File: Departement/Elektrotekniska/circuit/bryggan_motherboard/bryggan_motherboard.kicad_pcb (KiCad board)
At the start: 2 copper layers, 68.6 x 74.9 mm, 8 parts, among them J1 Conn_01x02, J2 Conn_01x04, J3 RbPi connect, J4 Conn_01x04, J5 Conn_01x03, J6 Conn_01x03, U1 ULN2003

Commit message: KICAD clean
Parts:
- removed J6: Conn_01x03, Connectors_Terminal_Blocks:TerminalBlock_bornier-3_P5.08mm
- added REF**: 1pin, Connectors:1pin, F.Cu at (203.2, 74.9)
- added REF**: 1pin, Connectors:1pin, F.Cu at (142.2, 74.9)
- added REF**: 1pin, Connectors:1pin, F.Cu at (142.2, 142.2)
- added REF**: 1pin, Connectors:1pin, F.Cu at (203.2, 142.2)
- J1: footprint Connectors_Terminal_Blocks:TerminalBlock_bornier-2_P5.08mm -> TerminalBlocks_Phoenix:TerminalBlock_Phoenix_PT-3.5mm_2pol
- J2, J4: footprint Connectors_Terminal_Blocks:TerminalBlock_bornier-4_P5.08mm -> TerminalBlocks_Phoenix:TerminalBlock_Phoenix_PT-3.5mm_4pol
- J5: value Conn_01x03 -> RJ45; footprint Connectors_Terminal_Blocks:TerminalBlock_bornier-3_P5.08mm -> Connectors:RJ45_8
- moved J5 15.3 mm to (190.5, 94.0), turned to 90 degrees
- moved J4 10.2 mm to (184.2, 135.9), turned to 0 degrees
- moved J2 6.35 mm to (167.6, 135.9), turned to 0 degrees
- moved J1 3.81 mm to (148.6, 132.1), turned to 270 degrees
- moved R1 2.54 mm to (179.1, 85.1), turned to 270 degrees
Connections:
- J2 pad 1: Net-(J1-Pad1) -> Net-(J1-Pad2)
- J2 pad 2: Net-(J1-Pad1) -> Net-(J1-Pad2)
- J2 pad 3: Net-(J1-Pad1) -> Net-(J1-Pad2)
- J2 pad 4: Net-(J1-Pad1) -> Net-(J1-Pad2)
- J3 pad 10: Net-(J1-Pad2) -> Net-(J1-Pad1)
- J5 pad 1: Net-(J3-Pad5) -> Net-(J3-Pad1)
- J5 pad 2: Net-(J3-Pad3) -> Net-(J3-Pad1)
- J5 pad 3: Net-(J3-Pad1) -> Net-(J5-Pad3)
- R1 pad 1: Net-(J3-Pad3) -> Net-(J3-Pad5)
- R1 pad 2: Net-(J3-Pad5) -> Net-(J3-Pad3)
- U1 pad 10: Net-(J4-Pad4) -> Net-(J4-Pad1)
- U1 pad 11: Net-(J4-Pad3) -> Net-(J4-Pad2)
- U1 pad 12: Net-(J4-Pad2) -> Net-(J4-Pad3)
- U1 pad 13: Net-(J4-Pad1) -> Net-(J4-Pad4)
- U1 pad 8: Net-(J1-Pad2) -> Net-(J1-Pad1)
- U1 pad 9: Net-(J1-Pad1) -> Net-(J1-Pad2)
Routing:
- net Net-(J4-Pad1): track 33.0 -> 1.27 mm
- net Net-(J4-Pad2): track 30.5 -> 1.27 mm
- net Net-(J4-Pad3): track 27.9 -> 1.27 mm
- net Net-(J4-Pad4): track 25.4 -> 1.27 mm
- net Net-(J1-Pad2): track 47.1 -> 23.7 mm
- net Net-(J3-Pad5): track 42.4 -> 30.8 mm
- net Net-(J3-Pad3): track 34.1 -> 24.2 mm
- net Net-(J3-Pad1): track 26.5 -> 18.1 mm
- net (no net): track 2.54 -> 0.00 mm
- net Net-(J1-Pad1): track 49.1 -> 47.1 mm

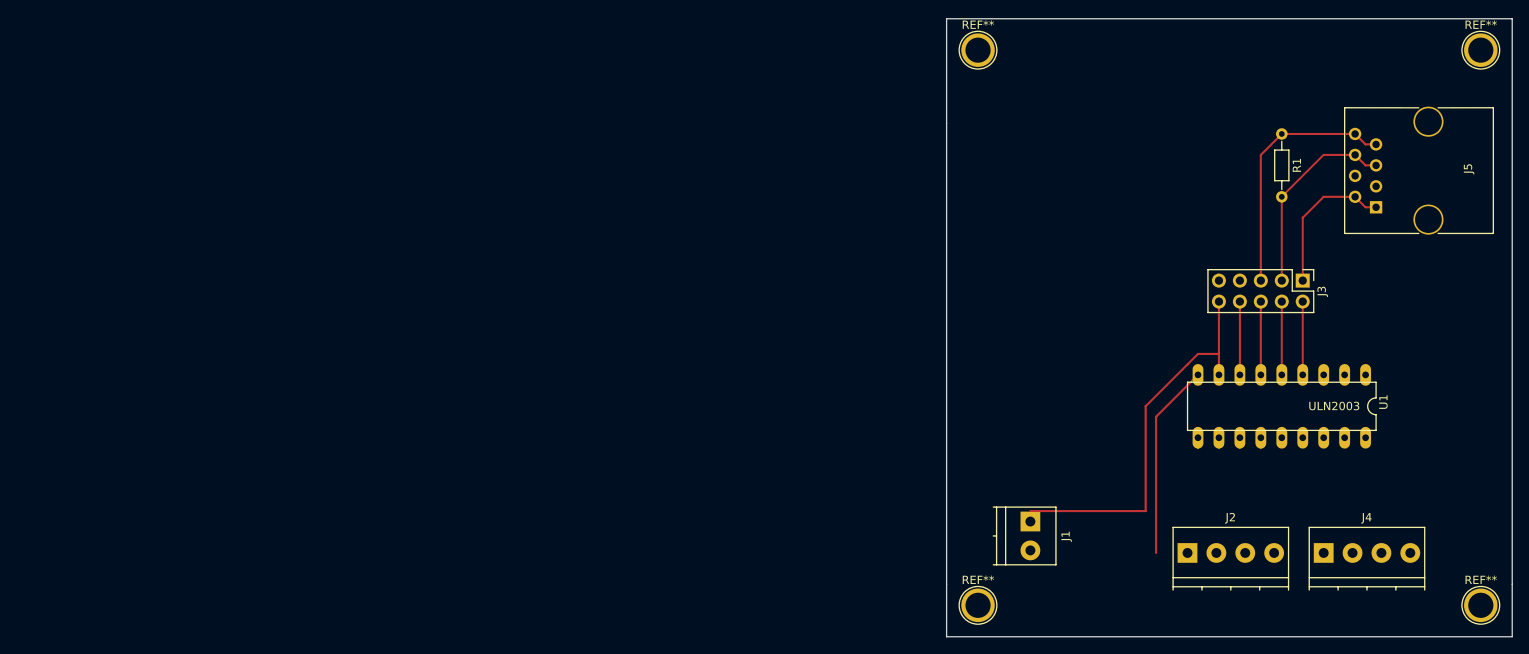
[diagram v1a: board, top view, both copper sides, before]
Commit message: RAW PIHAT TEMPLATE REMAKE
Template taken from: https://www.instructables.com/id/Design-a-Raspberry-Pi-Hat-KiCad/
No changes made, except replacing outdated components
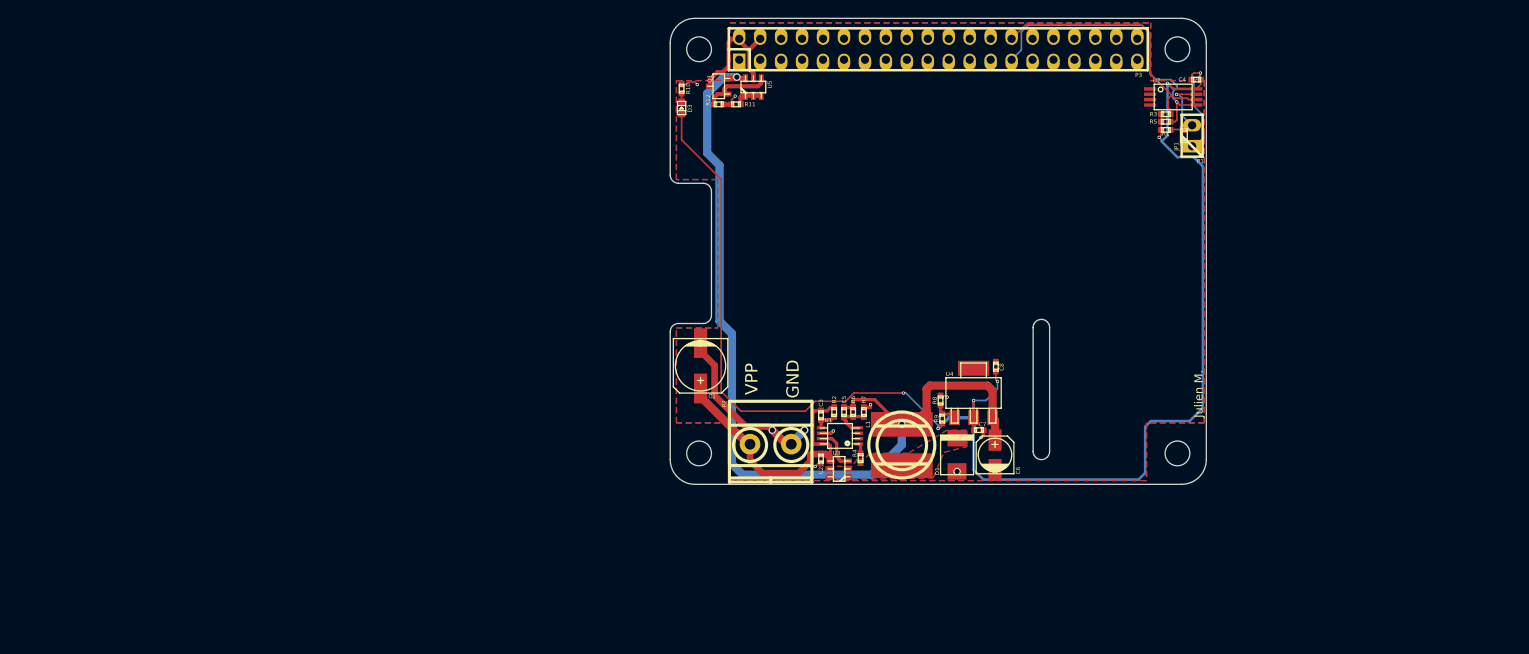
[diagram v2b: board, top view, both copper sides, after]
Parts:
- removed J1: Conn_01x02, TerminalBlocks_Phoenix:TerminalBlock_Phoenix_PT-3.5mm_2pol
- removed J2, J4: Conn_01x04, TerminalBlocks_Phoenix:TerminalBlock_Phoenix_PT-3.5mm_4pol
- removed J3: RbPi connect, Pin_Headers:Pin_Header_Straight_2x05_Pitch2.54mm
- removed J5: RJ45, Connectors:RJ45_8
- removed the REF** at (203.2, 74.9)
- removed the REF** at (142.2, 74.9)
- removed the REF** at (142.2, 142.2)
- removed the REF** at (203.2, 142.2)
- added C1: 50uf/50v, w_smd_cap:c_elec_6.3x7.7, F.Cu at (108.6, 113.2)
- added C2: 0.1uf, w_smd_cap:c_0402, F.Cu at (123.2, 124.4)
- added C3: 1nf, w_smd_cap:c_0402, F.Cu at (123.2, 119.2)
- added C4: 0.1uf, w_smd_cap:c_0402, F.Cu at (168.7, 78.5)
- added C5: 0.1uf, w_smd_cap:c_0402, F.Cu at (126.0, 118.8)
- added C6: 10uf/6.3V, w_smd_cap:c_elec_4x5.3, F.Cu at (144.3, 124.0)
- added C7: 0.1uf, w_smd_cap:c_0402, F.Cu at (142.3, 121.0)
- added C8: 1uf, w_smd_cap:c_0402, F.Cu at (144.4, 113.3)
- added D1: DIODESCH, w_smd_diode:do214aa, F.Cu at (139.7, 124.0)
- added D3: LED, w_smd_leds:Led_0603, F.Cu at (106.3, 81.9)
- added JP1: JUMPER, w_smd_resistors:r_0603, F.Cu at (167.2, 85.3)
- added L1: 22uH, w_smd_inductors:inductor_smd_8x5mm, F.Cu at (133.0, 122.8)
- added P1: CONN_01X02, w_pin_strip:pin_strip_2, F.Cu at (168.2, 85.3)
- added P2: CONN_01X02, w_conn_mkds:mkds_1,5-2, F.Cu at (117.1, 122.7)
- added P3: Raspberry_Pi_+_Conn, w_pin_strip:pin_socket_20x2, F.Cu at (137.4, 74.8)
- added Q1: BSS138, w_smd_trans:sot23, F.Cu at (110.8, 79.3)
- added R10: 360, w_smd_resistors:r_0402, F.Cu at (106.3, 79.6)
- added R11: 10k, w_smd_resistors:r_0402, F.Cu at (112.9, 81.5)
- added R12: 47k, w_smd_resistors:r_0402, F.Cu at (110.8, 81.5)
- added R2: 24k, w_smd_resistors:r_0402, F.Cu at (124.8, 118.8)
- added R3: 3.9k, w_smd_resistors:r_0402, F.Cu at (165.0, 82.7)
- added R4: 270, w_smd_resistors:r_0402, F.Cu at (128.0, 124.4)
- added R5: 3.9k, w_smd_resistors:r_0402, F.Cu at (165.0, 83.6)
- added R6: 30k, w_smd_resistors:r_0402, F.Cu at (127.1, 118.8)
- added R7: 10k, w_smd_resistors:r_0402, F.Cu at (128.4, 118.8)
- added R8: 390, w_smd_resistors:r_0402, F.Cu at (137.7, 117.4)
- added R9: 240, w_smd_resistors:r_0402, F.Cu at (137.9, 119.6)
- added REF**: MountingHole_3mm, Mounting_Holes:MountingHole_3mm, F.Cu at (166.4, 74.8)
- added REF**: MountingHole_3mm, Mounting_Holes:MountingHole_3mm, F.Cu at (166.4, 123.8)
- added REF**: MountingHole_3mm, Mounting_Holes:MountingHole_3mm, F.Cu at (108.4, 123.8)
- added REF**: MountingHole_3mm, Mounting_Holes:MountingHole_3mm, F.Cu at (108.4, 74.8)
- added U2: CAT24C32HU4I-GT3, w_smd_dil:tssop-8, F.Cu at (165.9, 80.6)
- added U3: FDC5614P, w_smd_trans:sot23-6, F.Cu at (125.4, 125.7)
- added U4: LM1117IMPX-ADJ, w_smd_trans:sot223, F.Cu at (141.7, 116.5)
- added U5: DMMT5401, w_smd_trans:sot23-6, F.Cu at (115.0, 79.4)
- R1: value R -> 1k; footprint Resistors_THT:R_Axial_DIN0204_L3.6mm_D1.6mm_P7.62mm_Horizontal -> w_smd_resistors:r_0402
- U1: value ULN2003 -> LM3489; footprint ULN2003:DIP18 -> w_smd_dil:msoic-8
- moved U1 53.7 mm to (125.5, 121.7), turned to 90 degrees
- moved R1 14.1 mm to (165.0, 84.6), turned to 180 degrees
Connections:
- R1 pad 1: Net-(J3-Pad5) -> +3V3
- U1 pad 2: Net-(U1-Pad2) -> GND
- U1 pad 6: Net-(J3-Pad6) -> GND
- U1 pad 8: Net-(J1-Pad1) -> +24V
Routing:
- net +3V3: track 0.00 -> 176.1 mm, vias 0 -> 6
- net +5V: track 0.00 -> 108.0 mm, vias 0 -> 2
- net Net-(J1-Pad1): track 47.1 -> 0.00 mm
- net GND: track 0.00 -> 44.4 mm, vias 0 -> 13
- net Net-(P3-Pad27): track 0.00 -> 36.9 mm, vias 0 -> 1
- net +24V: track 0.00 -> 35.0 mm
- net Net-(P3-Pad28): track 0.00 -> 32.4 mm
- net Net-(J3-Pad5): track 30.8 -> 0.00 mm
- net Net-(J1-Pad2): track 23.7 -> 0.00 mm
- net Net-(J3-Pad1): track 18.1 -> 0.00 mm
- net /Back Power Protection/5V_MCU: track 0.00 -> 15.5 mm
- net Net-(JP1-Pad1): track 24.2 -> 10.0 mm, vias 0 -> 1
- net Net-(J3-Pad6): track 8.89 -> 0.00 mm
- net Net-(Q1-Pad1): track 0.00 -> 8.73 mm
- net Net-(C3-Pad2): track 8.89 -> 2.74 mm
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- added copper zone on B.Cu, net GND
- added copper zone on F.Cu, net GND
- added copper zone on F.Cu, net Net-(D1-Pad2)
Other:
- board size 68.6 x 74.9 mm -> 65 x 56.5 mm
- net class Default: clearance 0.2 -> 0.15; trace_width 0.25 -> 0.2; via_dia 0.6 -> 0.889; via_drill 0.4 -> 0.635
- rule pad_to_mask_clearance: 0.2 -> 0
- rule trace_clearance: 0.2 -> 0.15
- rule trace_min: 0.2 -> 0.1
- rule via_min_drill: 0.3 -> 0.16
- rule via_min_size: 0.4 -> 0.26
- board text added: "CERN OHL V1.2"
- board text added: "GND"
- board text added: "Julien M."
- board text added: "VPP"

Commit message: Components added to board
Schematic RbPi to component fixed. No outgoing to full enclosure
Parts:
- removed C1: 50uf/50v, w_smd_cap:c_elec_6.3x7.7
- removed C2, C4, C5, C7: 0.1uf, w_smd_cap:c_0402
- removed C3: 1nf, w_smd_cap:c_0402
- removed C6: 10uf/6.3V, w_smd_cap:c_elec_4x5.3
- removed C8: 1uf, w_smd_cap:c_0402
- removed D1: DIODESCH, w_smd_diode:do214aa
- removed D3: LED, w_smd_leds:Led_0603
- removed JP1: JUMPER, w_smd_resistors:r_0603
- removed L1: 22uH, w_smd_inductors:inductor_smd_8x5mm
- removed P1: CONN_01X02, w_pin_strip:pin_strip_2
- removed P2: CONN_01X02, w_conn_mkds:mkds_1,5-2
- removed R10: 360, w_smd_resistors:r_0402
- removed R2: 24k, w_smd_resistors:r_0402
- removed R3, R5: 3.9k, w_smd_resistors:r_0402
- removed R4: 270, w_smd_resistors:r_0402
- removed R6: 30k, w_smd_resistors:r_0402
- removed R7: 10k, w_smd_resistors:r_0402
- removed R8: 390, w_smd_resistors:r_0402
- removed R9: 240, w_smd_resistors:r_0402
- removed U2: CAT24C32HU4I-GT3, w_smd_dil:tssop-8
- removed U3: FDC5614P, w_smd_trans:sot23-6
- removed U4: LM1117IMPX-ADJ, w_smd_trans:sot223
- added J1: RJ12, Connectors:RJ12_E, F.Cu at (119.7, 96.6)
- R1: value 1k -> 4.7k; footprint w_smd_resistors:r_0402 -> Resistors_THT:R_Axial_DIN0207_L6.3mm_D2.5mm_P7.62mm_Horizontal
- U1: value LM3489 -> ULN2003A; footprint w_smd_dil:msoic-8 -> ULN2003:DIP18
- moved R1 39.2 mm to (127.3, 95.3), turned to 270 degrees
- moved U1 38.8 mm to (153.9, 95.3), turned to 180 degrees
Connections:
- P3 pad 1: Net-(P3-Pad1) -> /+3.3V
- P3 pad 29: Net-(P3-Pad29) -> /HEAT_GPIO_PWM
- P3 pad 31: Net-(P3-Pad31) -> /PUMP1_GPIO_PWM
- P3 pad 32: Net-(P3-Pad32) -> /PUMP2_GPIO_PWM
- P3 pad 33: Net-(P3-Pad33) -> /FAN_GPIO
- P3 pad 7: Net-(P3-Pad7) -> /TEMP_GPIO
- R1 pad 1: +3V3 -> /+3.3V
- R1 pad 2: Net-(JP1-Pad1) -> /TEMP_GPIO
- U1 pad 1: Net-(R4-Pad2) -> /HEAT_GPIO_PWM
- U1 pad 2: GND -> /PUMP1_GPIO_PWM
- U1 pad 3: Net-(U1-Pad3) -> /PUMP2_GPIO_PWM
- U1 pad 4: Net-(C5-Pad2) -> /FAN_GPIO
- U1 pad 6: GND -> Net-(U1-Pad6)
- U1 pad 8: +24V -> GND
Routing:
- net (no net): track 0.00 -> 212.2 mm, vias 0 -> 16
- net +3V3: track 176.1 -> 0.00 mm, vias 6 -> 0
- net GND: track 44.4 -> 2.19 mm, vias 13 -> 1
- net +24V: track 35.0 -> 0.00 mm
- net Net-(JP1-Pad1): track 10.0 -> 0.00 mm, vias 1 -> 0
- net Net-(P3-Pad28): track 32.4 -> 22.8 mm
- net Net-(P3-Pad27): track 36.9 -> 27.9 mm, vias 1 -> 0
- net Net-(U1-Pad7): track 5.38 -> 0.00 mm
- net Net-(C5-Pad2): track 5.06 -> 0.00 mm
- net Net-(R8-Pad1): track 2.87 -> 0.00 mm
- net Net-(U1-Pad5): track 2.74 -> 0.00 mm
- net Net-(R4-Pad2): track 1.26 -> 0.00 mm
- net Net-(D3-Pad2): track 1.05 -> 0.00 mm

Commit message: Trans array footprint and wiring
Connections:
- net /TEMP_GPIO renamed /TEMP_GPIO_4
- net Net-(U1-Pad7) renamed /HEAT_GPIO_13_PWM
- P3 pad 12: Net-(P3-Pad12) -> /PUMP1_GPIO_18_PWM
- P3 pad 29: /HEAT_GPIO_PWM -> Net-(P3-Pad29)
- P3 pad 31: /PUMP1_GPIO_PWM -> Net-(P3-Pad31)
- P3 pad 32: /PUMP2_GPIO_PWM -> Net-(P3-Pad32)
- P3 pad 33: /FAN_GPIO -> /HEAT_GPIO_PWM_13
- P3 pad 35: Net-(P3-Pad35) -> /PUMP2_GPIO_19
- P3 pad 36: Net-(P3-Pad36) -> /FAN_GPIO_16
- P3 pad 37: Net-(P3-Pad37) -> /GPIO_26
- P3 pad 38: (no net) -> /GPIO_20
- P3 pad 40: Net-(P3-Pad40) -> /GPIO_21
- U1 pad 1: /HEAT_GPIO_PWM -> /GPIO_21
- U1 pad 2: /PUMP1_GPIO_PWM -> /GPIO_20
- U1 pad 3: /PUMP2_GPIO_PWM -> /GPIO_26
- U1 pad 4: /FAN_GPIO -> /FAN_GPIO_16
- U1 pad 5: Net-(U1-Pad5) -> /PUMP2_GPIO_19
- U1 pad 6: Net-(U1-Pad6) -> /PUMP1_GPIO_18_PWM

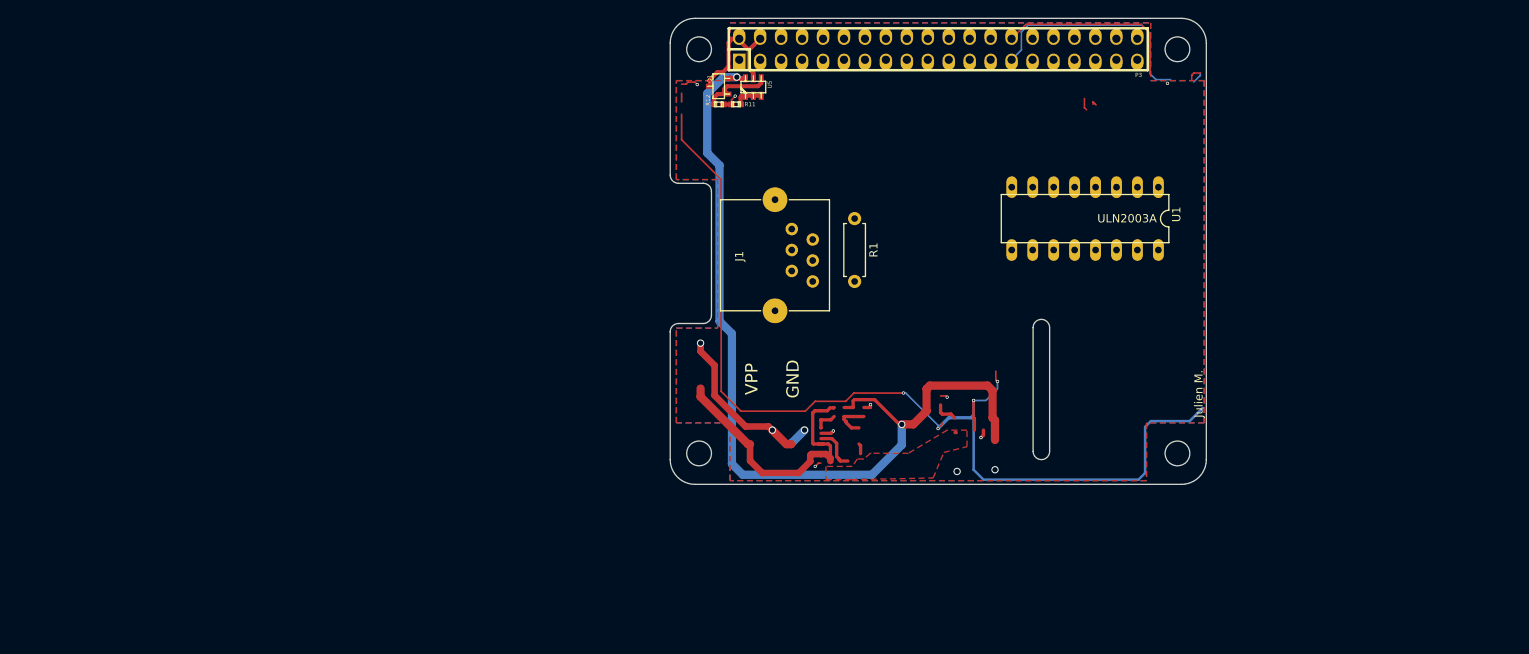
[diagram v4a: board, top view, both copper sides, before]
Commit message: PCB v0.9 finished
- Ground plane
- Barrel jack
- All tracks
- PCBNew Error check OK
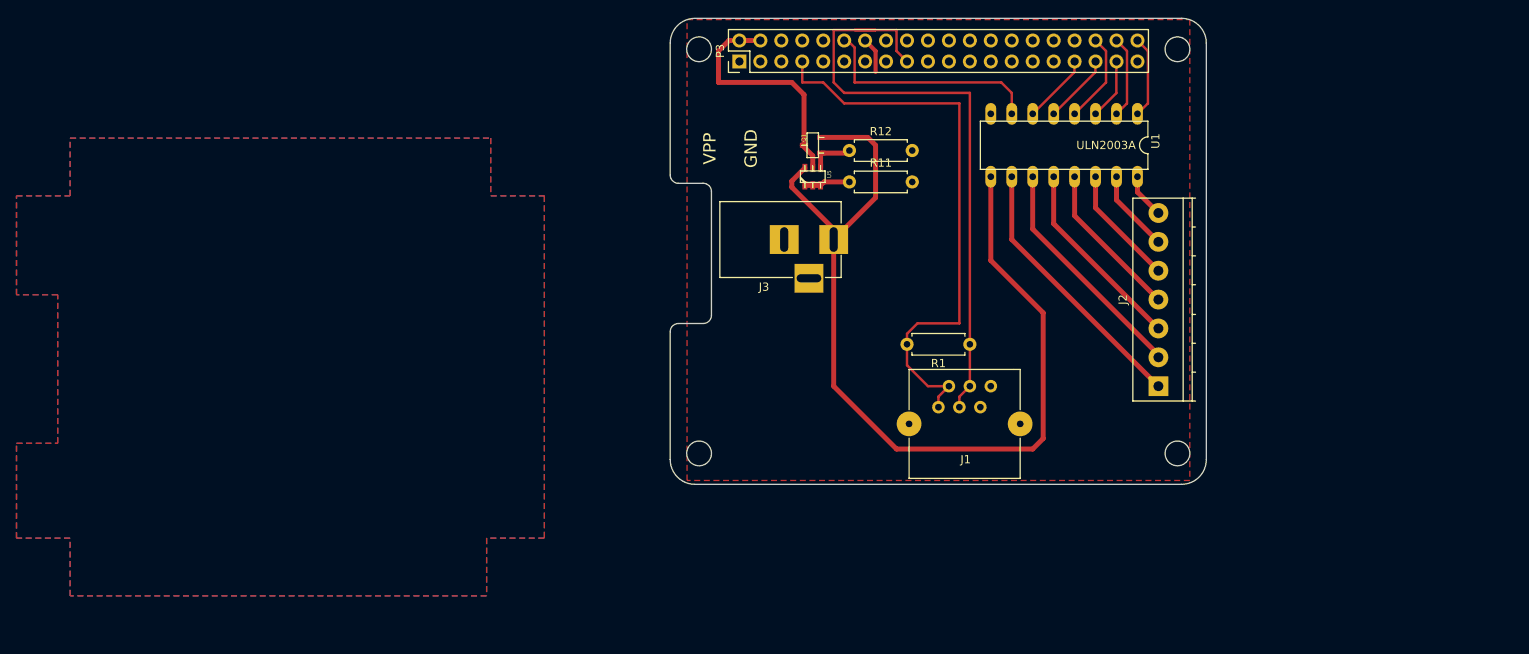
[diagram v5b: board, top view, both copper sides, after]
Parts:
- added J2: Screw_Terminal_01x07, TerminalBlocks_Phoenix:TerminalBlock_Phoenix_PT-3.5mm_7pol, F.Cu at (164.1, 115.7)
- added J3: Barrel_Jack, Connectors:BARREL_JACK, F.Cu at (124.7, 97.9)
- P3: footprint w_pin_strip:pin_socket_20x2 -> Pin_Headers:Pin_Header_Straight_2x20_Pitch2.54mm
- R11, R12: footprint w_smd_resistors:r_0402 -> Resistors_THT:R_Axial_DIN0207_L6.3mm_D2.5mm_P7.62mm_Horizontal
- moved J1 28.0 mm to (137.4, 118.2), turned to 0 degrees
- moved P3 24.2 mm to (113.3, 76.3), turned to 90 degrees
- moved R1 20.7 mm to (141.2, 110.6), turned to 180 degrees
- moved R12 16.8 mm to (126.6, 87.1), turned to 0 degrees
- moved R11 16.7 mm to (126.6, 90.9)
- moved Q1 13.5 mm to (122.2, 86.5)
- moved U5 13.0 mm to (122.2, 90.3)
- moved U1 9.25 mm to (151.4, 86.5)
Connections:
- J1 pad 1: /+3.3V -> /TEMP_GPIO_4
- J1 pad 2: /+3.3V -> /TEMP_GPIO_4
- J1 pad 3: /TEMP_GPIO_4 -> /+3.3V
- J1 pad 4: /TEMP_GPIO_4 -> /+3.3V
- P3 pad 1: /+3.3V -> Net-(P3-Pad1)
- P3 pad 12: /PUMP1_GPIO_18_PWM -> /HEAT_GPIO_13_PWM
- P3 pad 14: GND -> Net-(P3-Pad14)
- P3 pad 17: Net-(P3-Pad17) -> /+3.3V
- P3 pad 25: GND -> Net-(P3-Pad25)
- P3 pad 30: GND -> Net-(P3-Pad30)
- P3 pad 33: /HEAT_GPIO_PWM_13 -> /PUMP1_GPIO_18_PWM
- P3 pad 34: GND -> Net-(P3-Pad34)
- P3 pad 39: GND -> Net-(P3-Pad39)
- P3 pad 6: GND -> Net-(P3-Pad6)
- P3 pad 9: GND -> Net-(P3-Pad9)
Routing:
- net (no net): track 212.2 -> 0.00 mm, vias 16 -> 0
- net /+3.3V: track 0.00 -> 79.0 mm
- net /TEMP_GPIO_4: track 0.00 -> 69.2 mm
- net Net-(J2-Pad1): track 0.00 -> 32.8 mm
- net Net-(J2-Pad2): track 0.00 -> 28.2 mm
- net /HEAT_GPIO_13_PWM: track 0.00 -> 28.1 mm
- net Net-(P3-Pad27): track 27.9 -> 0.00 mm
- net Net-(J2-Pad3): track 0.00 -> 23.7 mm
- net Net-(P3-Pad28): track 22.8 -> 0.00 mm
- net Net-(J2-Pad4): track 0.00 -> 19.1 mm
- net Net-(J2-Pad5): track 0.00 -> 14.6 mm
- net /Back Power Protection/5V_MCU: track 15.5 -> 30.0 mm
- net /FAN_GPIO_16: track 0.00 -> 11.2 mm
- net /GPIO_20: track 0.00 -> 10.2 mm
- net /GPIO_21: track 0.00 -> 10.2 mm
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- removed copper zone on F.Cu, net Net-(D1-Pad2)
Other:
- outline, holes or cut-outs redrawn
- board text removed: "Julien M."
